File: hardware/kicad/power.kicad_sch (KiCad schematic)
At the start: 49 parts, among them U1 LFE5U-25F-6BG381C, U3 TLV62569DBV, U4 TLV62569DBV, U5 TLV62569DBV

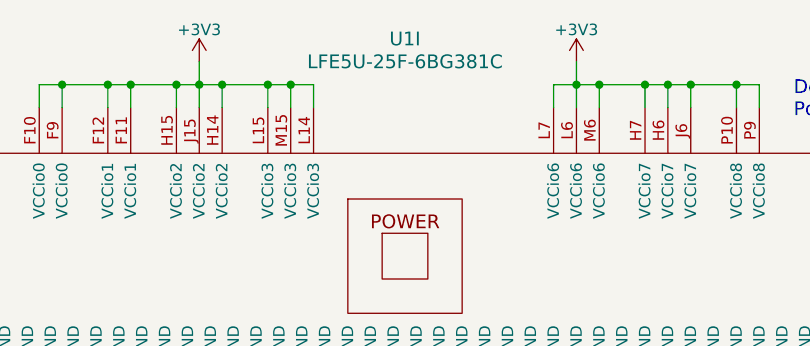
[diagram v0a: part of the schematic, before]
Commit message: Updates FPGA model in BOM and schematics
Replaces LFE5U-25F-6BG381C with LFE5U-85F-8BG381I in multiple files.
Ensures consistency across BOM, schematics, and PCB layouts for the updated FPGA model.
Adjusts related properties such as part number and connectivity attributes.

Addresses a hardware specification upgrade in branch 1.1.
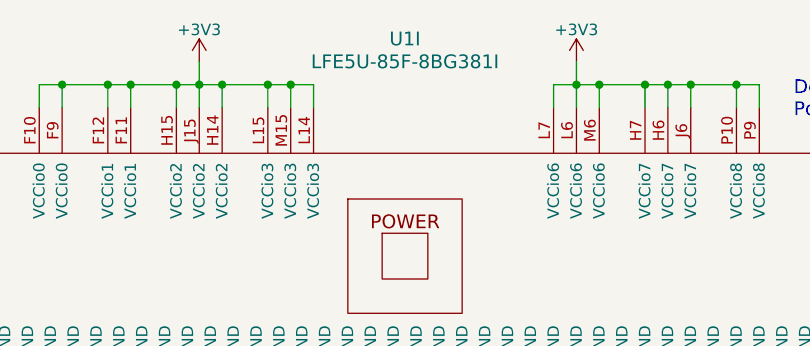
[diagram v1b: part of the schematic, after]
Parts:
- U1: value LFE5U-25F-6BG381C -> LFE5U-85F-8BG381I; MPN LFE5U-85F-6BG381C -> LFE5U-85F-8BG381I
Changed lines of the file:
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@@
 			)
 		)
-		(property "Value" "LFE5U-25F-6BG381C"
+		(property "Value" "LFE5U-85F-8BG381I"
 			(at 157.48 26.67 0)
 			(effects
@@
 			)
 		)
-		(property "MPN" "LFE5U-85F-6BG381C"
+		(property "MPN" "LFE5U-85F-8BG381I"
 			(at 157.48 48.26 0)
 			(effects
